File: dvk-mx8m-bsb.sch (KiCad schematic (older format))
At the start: 14 parts, among them J101 IMX8M-SOM, J102 TEST_1P

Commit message: Add Proximity+Ambient Light sensor and 9-axis IMU circuits to the "sensors" schematic sheet, include the associated footprints and assign them to the respective symbols
The 9-axis IMU is configured to use I2C(1) rather than SPI. Notes are included regarding the IMU's setup. Descriptions of the IMU state that it is "fully compliant with Android" and therefore drivers must be available.
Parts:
- C103, C104: value 0.1uF -> 100nF
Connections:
- no-connect marks 87 -> 89
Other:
- note added: "TODO:\nGNSS\nNOR Flash\nMIPI DSI/CSI"
- note removed: "TODO:\nGNSS\nNOR Flash\n9-axis\nSensors\nMIPI DSI/CSI"
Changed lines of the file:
@@
 $Descr A2 23386 16535
 encoding utf-8
-Sheet 1 18
+Sheet 1 19
 Title "DVK-MX8M-BSB"
 Date "2018-05-02"
@@
 P 11100 13250
 F 0 "C103" H 11125 13350 50  0000 L CNN
-F 1 "0.1uF" H 11125 13150 50  0000 L CNN
+F 1 "100nF" H 11125 13150 50  0000 L CNN
 F 2 "" H 11138 13100 50  0001 C CNN
 F 3 "" H 11100 13250 50  0001 C CNN
@@
 P 12300 13250
 F 0 "C104" H 12325 13350 50  0000 L CNN
-F 1 "0.1uF" H 12325 13150 50  0000 L CNN
+F 1 "100nF" H 12325 13150 50  0000 L CNN
 F 2 "" H 12338 13100 50  0001 C CNN
 F 3 "" H 12300 13250 50  0001 C CNN
@@
 	11450 11850 11350 11850
 Wire Wire Line
-	11350 13050 11350 11850
+	11350 11850 11350 13050
 Wire Wire Line
 	10600 13050 11450 13050
@@
 MIC_SEL
 NoConn ~ 7800 3000
-Text Notes 5150 14750 0    60   ~ 0
-TODO:\nGNSS\nNOR Flash\n9-axis\nSensors\nMIPI DSI/CSI
+Text Notes 5150 15200 0    60   ~ 0
+TODO:\nGNSS\nNOR Flash\nMIPI DSI/CSI
 $Sheet
 S 5150 11950 1400 1850
@@
 Text Label 19650 2650 2    60   ~ 0
 HDMI_HPD
+$Sheet
+S 5150 14000 1400 600
+U 5B05878C
+F0 "Sensors" 60
+F1 "sensors.sch" 60
+F2 "I2C1_SDA" B R 6550 14100 60
+F3 "I2C1_SCL" I R 6550 14200 60
+F4 "PROX_~INT" O R 6550 14350 60
+F5 "IMU_INT" O R 6550 14500 60
+$EndSheet
+Wire Wire Line
+	6550 14100 7800 14100
+Wire Wire Line
+	6550 14200 7800 14200
+Wire Wire Line
+	6550 14350 7800 14350
+Wire Wire Line
+	6550 14500 7800 14500
+Text Label 7800 14100 2    60   ~ 0
+I2C1_SDA
+Text Label 7800 14200 2    60   ~ 0
+I2C1_SCL
+Text Label 7800 14350 2    60   ~ 0
+PROX_~INT
+Text Label 7800 14500 2    60   ~ 0
+IMU_INT
+NoConn ~ 7800 14350
+NoConn ~ 7800 14500
 $EndSCHEMATC

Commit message: Add NOR flash chip schematic, use mini-HDMI (requested) instead of micro and add its corresponding properties and footprint, use 3.5mm CTIA headset jack with through-hole pins rather than an SMD one for extra "mechanical rigidity"
Will likely want to use a USB-C receptacle with through-hole shield pins.
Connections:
- net ECSPI1_SCLK: now reaches J101.D26 (Pin_26)
- net ECSPI1_SS0: now reaches J101.D30 (Pin_30)
- net ECSPI1_MISO: now reaches J101.D51 (Pin_51)
- net ECSPI1_MOSI: now reaches J101.D65 (Pin_65)
- no-connect marks 89 -> 85
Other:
- note added: "TODO:\nVibration Motor\nGNSS\nMIPI DSI/CSI"
- note removed: "TODO:\nGNSS\nNOR Flash\nMIPI DSI/CSI"
- note removed: "TODO:\nneed a vibration motor?"

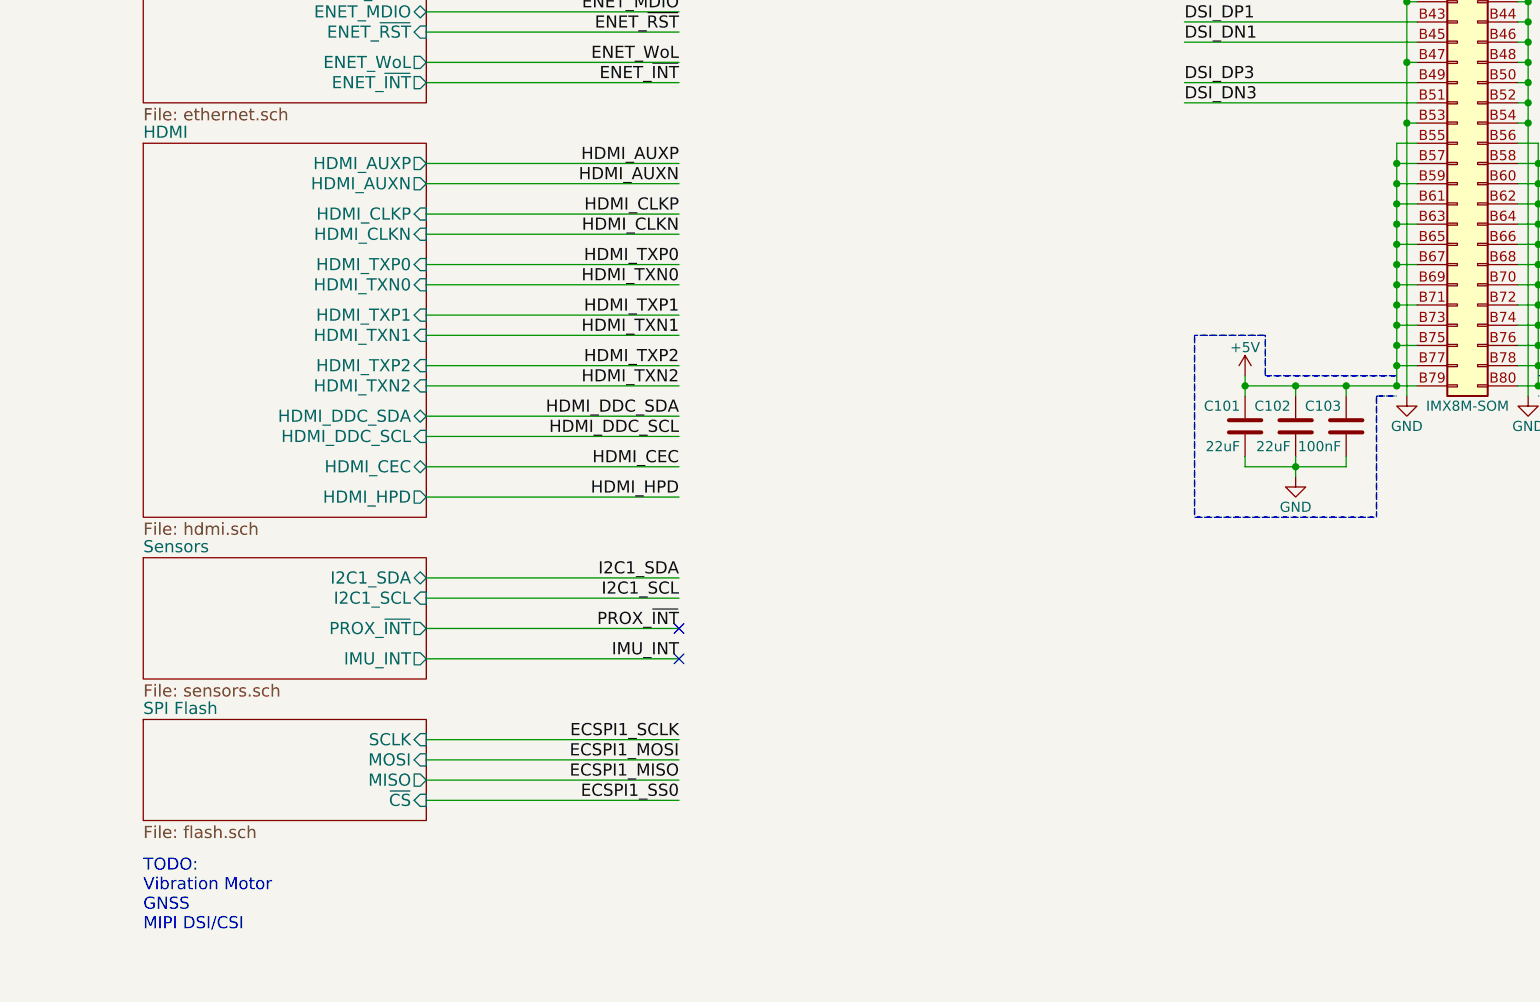
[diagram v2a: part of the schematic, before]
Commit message: Add haptic/vibration motor circuit
Using a PFET to switch the high-side. The motor will likely be coin-shaped with adhesive on the back to stick to a designated spot on the board and have a 2-pin Molex or JST connector installed on the wire leads (by request).
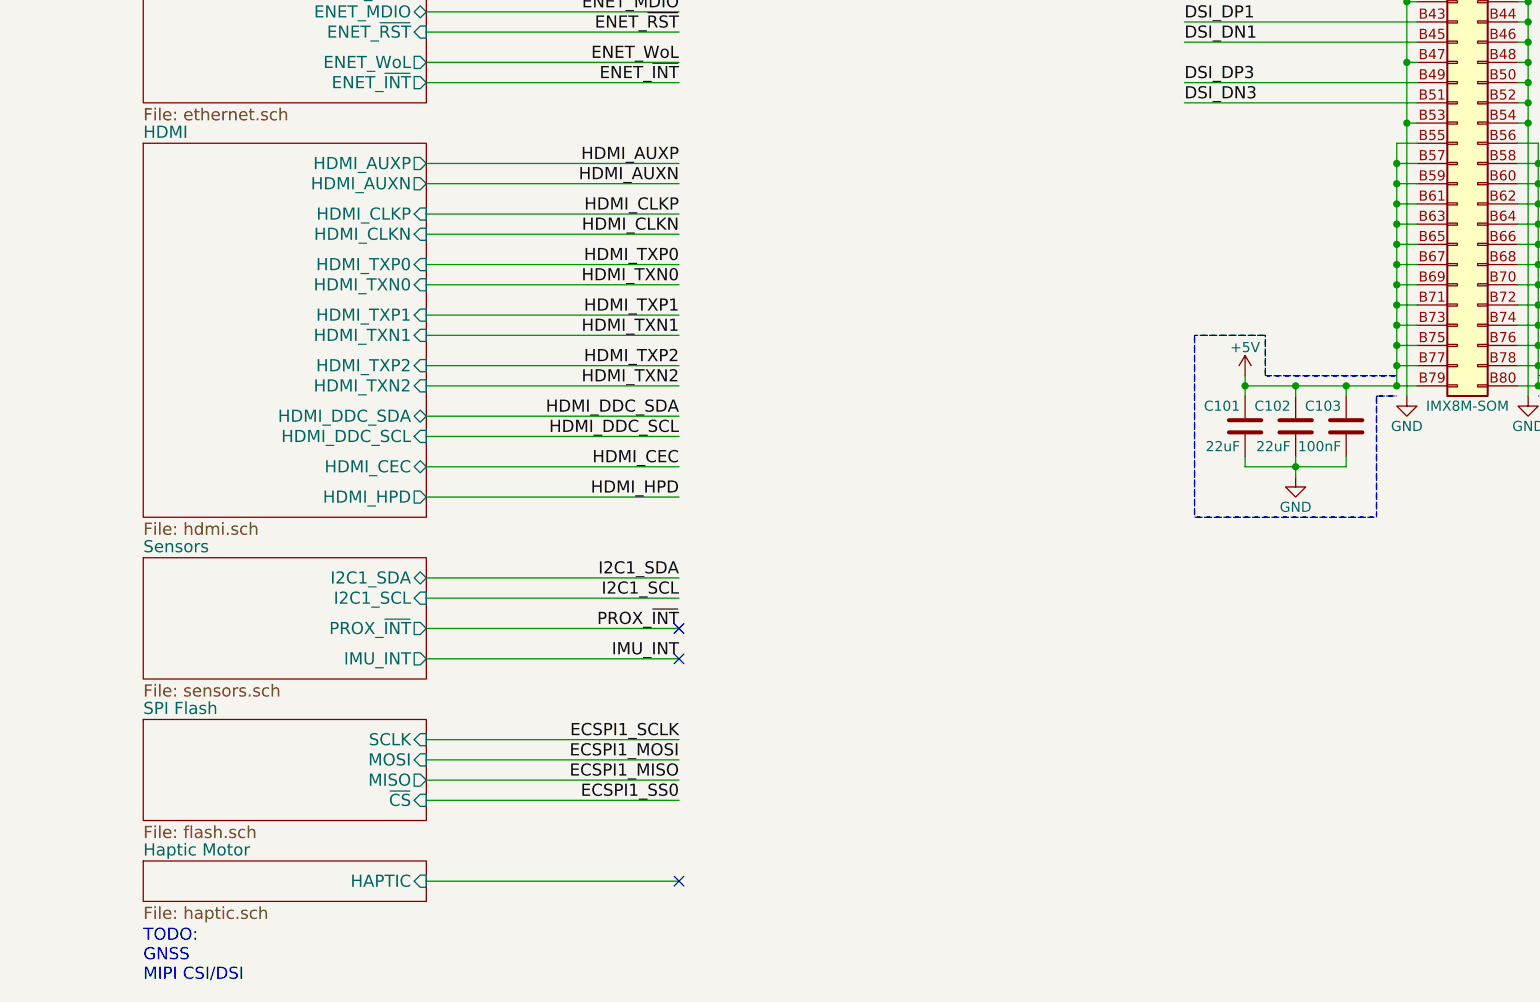
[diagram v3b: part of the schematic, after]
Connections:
- no-connect marks 85 -> 86
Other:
- note added: "TODO:\nGNSS\nMIPI CSI/DSI"
- note removed: "TODO:\nVibration Motor\nGNSS\nMIPI DSI/CSI"
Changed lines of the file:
@@
 $Descr A2 23386 16535
 encoding utf-8
-Sheet 1 20
+Sheet 1 21
 Title "DVK-MX8M-BSB"
-Date "2018-05-14"
+Date "2018-05-15"
 Rev "v0.1.0"
 Comp "Purism SPC"
@@
 	11450 11850 11350 11850
 Wire Wire Line
-	11350 13050 11350 11850
+	11350 11850 11350 13050
 Wire Wire Line
 	10600 13050 11450 13050
@@
 MIC_SEL
 NoConn ~ 7800 2900
-Text Notes 5150 15750 0    60   ~ 0
-TODO:\nVibration Motor\nGNSS\nMIPI DSI/CSI
+Text Notes 5150 16000 0    60   ~ 0
+TODO:\nGNSS\nMIPI CSI/DSI
 $Sheet
 S 5150 11850 1400 1850
@@
 Text Label 7800 14800 2    60   ~ 0
 ECSPI1_SCLK
+$Sheet
+S 5150 15400 1400 200
+U 5AFCB56A
+F0 "Haptic Motor" 60
+F1 "haptic.sch" 60
+F2 "HAPTIC" I R 6550 15500 60
+$EndSheet
+Wire Wire Line
+	6550 15500 7800 15500
+NoConn ~ 7800 15500
 $EndSCHEMATC

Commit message: Assign SAI5 to the WLAN/BT M.2, remove SIM2 slot due to conflicts between modules (specifically the L830-EB being a Config_0 module where the TX_BLANKING signal would connected to USIM_PWR2 sink), reassign the corresponding M.2 config pin to handle HP_DET, remove the AMOLED buck-boost as a different regulator will be used
The MIC_SEL, PROX_~INT, IMU_INT, and HAPTIC signals still need assigning
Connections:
- net SAI5_RXC(GPIO3_IO20) is gone; now on net HP_DET: J101.C53 (Pin_53)
- net SAI5_TX_BCLK: now reaches J101.C36 (Pin_36)
- net SAI5_RXD: now reaches J101.C43 (Pin_43)
- net SAI5_TX_SYNC: now reaches J101.C46 (Pin_46)
- net SAI5_TXD: now reaches J101.C61 (Pin_61)
- no-connect marks 86 -> 79
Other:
- note added: "SAI5_RXC(GPIO3_IO20)"
- note removed: "SAI6_RXD0!!!"
- note removed: "SAI6_TXC/RXC!!!"
- note removed: "SAI6_TXD0!!!"
- note removed: "SAI6_TXFS/RXFS!!!"
- note removed: "TODO:\nassign a SAI bus"
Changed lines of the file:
@@
 $EndSheet
 $Sheet
-S 6150 900  1400 1250
+S 6150 900  1400 1000
 U 5B0FA74B
 F0 "Power" 60
@@
 F2 "PWR_EN" I R 7550 1650 60
 F3 "SD2_~RST" I R 7550 1800 60
-F4 "SWIRE" I R 7550 1950 60
-F5 "AVDD_EN" I R 7550 2050 60
-F6 "VBAT_REG" I L 6150 1000 60
-F7 "+5V" O R 7550 1000 60
-F8 "3V3_P" O R 7550 1250 60
-F9 "1V8_P" O R 7550 1500 60
+F4 "VBAT_REG" I L 6150 1000 60
+F5 "+5V" O R 7550 1000 60
+F6 "3V3_P" O R 7550 1250 60
+F7 "1V8_P" O R 7550 1500 60
 $EndSheet
 Text Label 3200 5500 2    60   ~ 0
@@
 $EndSheet
 $Sheet
-S 550  12900 1400 1600
+S 550  12900 1400 1450
 U 5ACD5EDE
 F0 "WWAN M.2" 60
 F1 "wwan_m2.sch" 60
-F2 "CONFIG" O R 1950 13000 60
-F3 "UART_TX/LED" O R 1950 13600 60
-F4 "UART_RX/DPR" I R 1950 13700 60
-F5 "~WoWWAN" O R 1950 13150 60
-F6 "USB_D+" B R 1950 13850 60
-F7 "USB_D-" B R 1950 13950 60
-F8 "~W_DISABLE1" I R 1950 13300 60
-F9 "~RESET" I R 1950 13450 60
-F10 "PCM_SYNC/I2S_FSC" B R 1950 14200 60
-F11 "PCM_CLK/I2S_SCK" B R 1950 14100 60
-F12 "PCM_IN/I2S_IN" I R 1950 14300 60
-F13 "PCM_OUT/I2S_OUT" O R 1950 14400 60
+F2 "UART_TX/LED" O R 1950 13450 60
+F3 "UART_RX/DPR" I R 1950 13550 60
+F4 "~WoWWAN" O R 1950 13000 60
+F5 "USB_D+" B R 1950 13700 60
+F6 "USB_D-" B R 1950 13800 60
+F7 "~W_DISABLE1" I R 1950 13150 60
+F8 "~RESET" I R 1950 13300 60
+F9 "PCM_SYNC/I2S_FSC" B R 1950 14050 60
+F10 "PCM_CLK/I2S_SCK" B R 1950 13950 60
+F11 "PCM_IN/I2S_IN" I R 1950 14150 60
+F12 "PCM_OUT/I2S_OUT" O R 1950 14250 60
 $EndSheet
 $Sheet
@@
 Text Label 10300 11650 0    60   ~ 0
 DSI_DN3
-Text Label 8800 1950 2    60   ~ 0
-SWIRE
-Text Label 8800 2050 2    60   ~ 0
-AVDD_EN
 Text Label 3200 10950 2    60   ~ 0
 AVDD_EN
@@
 Text Label 3200 11500 2    60   ~ 0
 SAI1_RXD3(GPIO4_IO05)
-Text Label 3200 13000 2    60   ~ 0
-SAI5_RXC(GPIO3_IO20)
-Text Label 3200 13600 2    60   ~ 0
+Text Label 3200 13450 2    60   ~ 0
 UART3_RXD
-Text Label 3200 13700 2    60   ~ 0
+Text Label 3200 13550 2    60   ~ 0
 UART3_TXD
 Text Label 16850 11850 0    60   ~ 0
@@
 Text Label 16850 10850 0    60   ~ 0
 UART3_TXD
+Text Label 3200 13150 2    60   ~ 0
+~WWAN_DISABLE
 Text Label 3200 13300 2    60   ~ 0
-~WWAN_DISABLE
-Text Label 3200 13450 2    60   ~ 0
 GPIO3_IO09
-Text Notes 3250 13300 0    60   ~ 0
+Text Notes 3250 13150 0    60   ~ 0
 GPIO3_IO04
-Text Label 3200 13150 2    60   ~ 0
+Text Label 3200 13000 2    60   ~ 0
 GPIO3_IO08
 Text Label 13100 9450 2    60   ~ 0
@@
 GPIO3_IO09
 Text Label 16850 5250 0    60   ~ 0
-SAI5_RXC(GPIO3_IO20)
-Text Label 3200 14300 2    60   ~ 0
+HP_DET
+Text Label 3200 14150 2    60   ~ 0
 SAI1_RXD5(GPIO4_IO07)
-Text Notes 3250 14300 0    60   ~ 0
-SAI6_TXD0!!!
-Text Label 3200 14400 2    60   ~ 0
+Text Notes 3250 14150 0    60   ~ 0
+SAI6_TXD0
+Text Label 3200 14250 2    60   ~ 0
 SAI1_TXD5(GPIO4_IO17)
-Text Notes 3250 14400 0    60   ~ 0
-SAI6_RXD0!!!
-Text Label 3200 14200 2    60   ~ 0
+Text Notes 3250 14250 0    60   ~ 0
+SAI6_RXD0
+Text Label 3200 14050 2    60   ~ 0
 SAI1_RXD6(GPIO4_IO08)
-Text Notes 3250 14200 0    60   ~ 0
-SAI6_TXFS/RXFS!!!
-Text Label 3200 14100 2    60   ~ 0
+Text Notes 3250 14050 0    60   ~ 0
+SAI6_TXFS/RXFS
+Text Label 3200 13950 2    60   ~ 0
 SAI1_TXD4(GPIO4_IO16)
-Text Notes 3250 14100 0    60   ~ 0
-SAI6_TXC/RXC!!!
+Text Notes 3250 13950 0    60   ~ 0
+SAI6_TXC/RXC
 $Comp
 L IMX8M-SOM J101
@@
 Text Label 3200 9150 2    60   ~ 0
 USB_WLAN_DM
-Text Label 3200 13850 2    60   ~ 0
+Text Label 3200 13700 2    60   ~ 0
 USB_WWAN_DP
-Text Label 3200 13950 2    60   ~ 0
+Text Label 3200 13800 2    60   ~ 0
 USB_WWAN_DM
 Text Label 7800 4150 2    60   ~ 0
@@
 NoConn ~ 17900 9250
 NoConn ~ 17900 9350
-NoConn ~ 18600 4350
-NoConn ~ 18600 4850
 NoConn ~ 18600 5250
 NoConn ~ 18600 5450
@@
 NoConn ~ 17900 4450
 NoConn ~ 17900 3550
-NoConn ~ 17900 4750
 NoConn ~ 17900 4850
 NoConn ~ 17900 5050
 NoConn ~ 17900 5450
-NoConn ~ 17900 5650
 NoConn ~ 17900 6150
 NoConn ~ 11350 2750
@@
 Text Label 13100 6150 2    60   ~ 0
 ~WWAN_DISABLE
-Text Label 7800 6450 2    60   ~ 0
-M2_PCM_CLK
-Text Label 7800 6550 2    60   ~ 0
-M2_PCM_SYNC
-Text Label 7800 6650 2    60   ~ 0
-M2_PCM_IN
-Text Label 7800 6750 2    60   ~ 0
-M2_PCM_OUT
-NoConn ~ 7800 6450
-NoConn ~ 7800 6550
-NoConn ~ 7800 6650
-NoConn ~ 7800 6750
 Wire Wire Line
 	11950 9950 13100 9950
@@
 	11450 11650 10300 11650
 Wire Wire Line
-	7550 1950 8800 1950
-Wire Wire Line
-	7550 2050 8800 2050
-Wire Wire Line
 	1950 9800 3200 9800
 Wire Wire Line
@@
 	18000 3650 16850 3650
 Wire Wire Line
+	1950 13450 3200 13450
+Wire Wire Line
+	1950 13550 3200 13550
+Wire Wire Line
+	18000 11850 16850 11850
+Wire Wire Line
+	18000 10850 16850 10850
+Wire Wire Line
 	1950 13000 3200 13000
 Wire Wire Line
-	1950 13600 3200 13600
-Wire Wire Line
-	1950 13700 3200 13700
-Wire Wire Line
-	18000 11850 16850 11850
-Wire Wire Line
-	18000 10850 16850 10850
+	1950 13950 3200 13950
+Wire Wire Line
+	1950 14050 3200 14050
+Wire Wire Line
+	1950 14150 3200 14150
+Wire Wire Line
+	1950 14250 3200 14250
 Wire Wire Line
 	1950 13150 3200 13150
 Wire Wire Line
-	1950 14100 3200 14100
-Wire Wire Line
-	1950 14200 3200 14200
-Wire Wire Line
-	1950 14300 3200 14300
-Wire Wire Line
-	1950 14400 3200 14400
-Wire Wire Line
 	1950 13300 3200 13300
-Wire Wire Line
-	1950 13450 3200 13450
 Wire Wire Line
 	11950 9450 13100 9450
@@
 	1950 9150 3200 9150
 Wire Wire Line
-	1950 13850 3200 13850
-Wire Wire Line
-	1950 13950 3200 13950
+	1950 13700 3200 13700
+Wire Wire Line
+	1950 13800 3200 13800
 Wire Wire Line
 	6550 4150 7800 4150
@@
 	11950 5350 13100 5350
 Wire Wire Line
-	18500 4350 18600 4350
-Wire Wire Line
-	18500 4850 18600 4850
+	18500 4350 19650 4350
+Wire Wire Line
+	18500 4850 19650 4850
 Wire Wire Line
 	18500 5250 18600 5250
@@
 	18000 4450 17900 4450
 Wire Wire Line
-	18000 4750 17900 4750
+	18000 4750 16850 4750
 Wire Wire Line
 	18000 4850 17900 4850
@@
 	18000 5450 17900 5450
 Wire Wire Line
-	18000 5650 17900 5650
+	18000 5650 16850 5650
 Wire Wire Line
 	18000 6150 17900 6150
@@
 Text Label 19650 11150 2    60   ~ 0
 UART4_RXD
-NoConn ~ 7800 2750
-Text Notes 7900 6650 0    60   ~ 0
-TODO:\nassign a SAI bus
 Wire Wire Line
 	6550 3600 7800 3600
@@
 	6550 15500 7800 15500
 NoConn ~ 7800 15500
+Text Label 7800 6450 2    60   ~ 0
+SAI5_TX_BCLK
+Text Label 7800 6550 2    60   ~ 0
+SAI5_TX_SYNC
+Text Label 7800 6750 2    60   ~ 0
+SAI5_TXD
+Text Label 7800 6650 2    60   ~ 0
+SAI5_RXD
+Text Label 19650 4350 2    60   ~ 0
+SAI5_TX_BCLK
+Text Label 19650 4850 2    60   ~ 0
+SAI5_TX_SYNC
+Text Label 16850 4750 0    60   ~ 0
+SAI5_RXD
+Text Label 16850 5650 0    60   ~ 0
+SAI5_TXD
+Text Notes 7900 2750 0    60   ~ 0
+SAI5_RXC(GPIO3_IO20)
+NoConn ~ 3200 11050
+NoConn ~ 3200 10950
 $EndSCHEMATC

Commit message: Include power load switch ICs to the 3.3V and 5V rails so that the SoC can disable the peripherals' power using the PWR_EN signal
Need to verify that 3V3's capacitance is greater than 3V3_P!

Next step is to have PWR_EN control the various logic translator chips EN pins.
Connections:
- net +5V renamed 5V_SOM
- net 5V_SOM: no longer R105.1
- new net 5V_P: R105.1
